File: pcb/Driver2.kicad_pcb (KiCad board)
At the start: 2 copper layers, 78 x 124 mm, 27 parts, among them P1 CONN_2, P2 CONN_2, Q1 IRF540N, Q2 IRF540N, T1 ETD29, U1 ArdinoMinPro, U2 MCP14E3

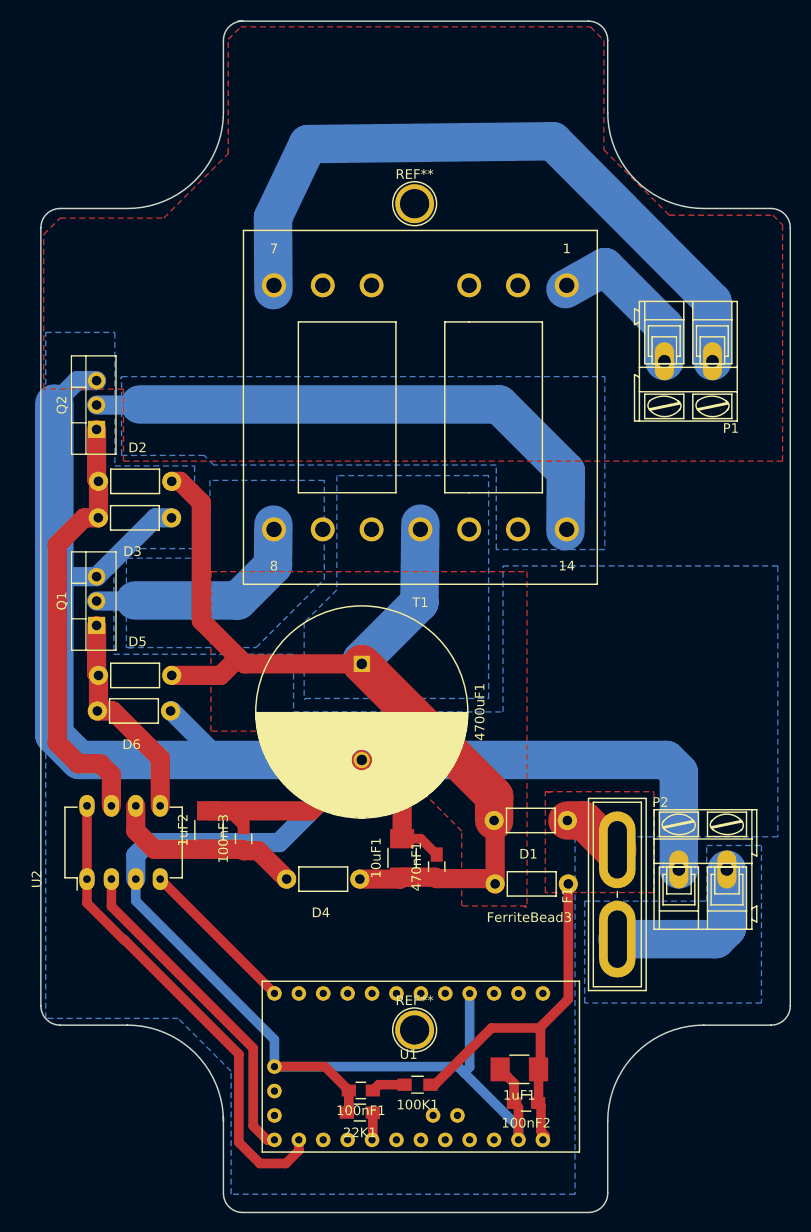
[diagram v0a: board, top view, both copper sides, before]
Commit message: Rev 1 working code, schematic updated, pcb todo
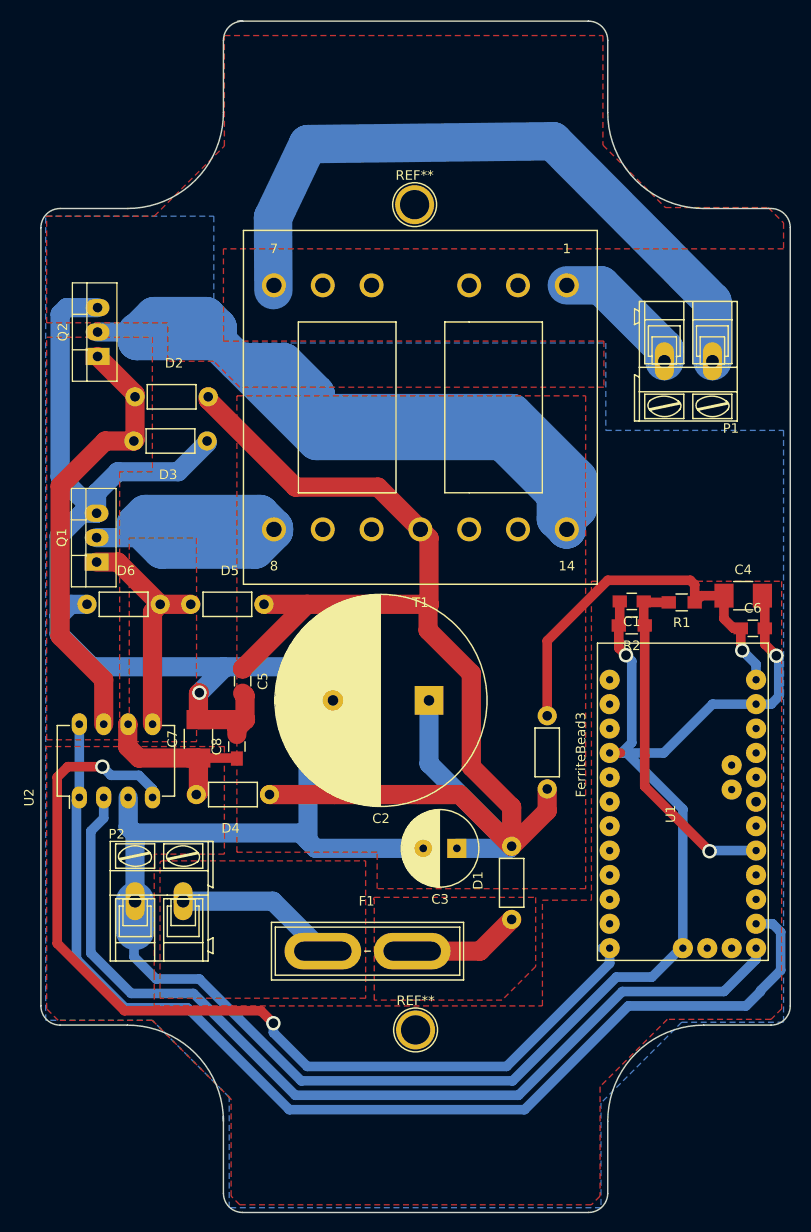
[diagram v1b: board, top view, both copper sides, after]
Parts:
- removed 100K1, 22K1: R, Resistors_SMD:R_0805_HandSoldering
- removed 100nF1, 100nF2, 100nF3, 470nF1: C, Capacitors_SMD:C_0805_HandSoldering
- removed 10uF1, 1uF1, 1uF2: CAPAPOL, Capacitors_SMD:C_1210_HandSoldering
- removed 4700uF1: CAPAPOL, Capacitors_ThroughHole:C_Radial_D22_L41_P10
- removed the REF** at (137.4, 160.5)
- removed the REF** at (137.4, 74.5)
- added C1: 100nF, Capacitors_SMD:C_0805_HandSoldering, F.Cu at (160.0, 115.9)
- added C2: 4700uF 50V, Capacitors_ThroughHole:C_Radial_D22_L41_P10, F.Cu at (138.9, 126.2)
- added C3: 330uF 50v, Capacitors_ThroughHole:C_Radial_D8_L11.5_P3.5, F.Cu at (141.8, 141.6)
- added C4: 1uF, Capacitors_SMD:C_1210_HandSoldering, F.Cu at (171.6, 115.3)
- added C5: 470nF, Capacitors_SMD:C_0805_HandSoldering, F.Cu at (119.5, 124.2)
- added C6: 100nF, Capacitors_SMD:C_0805_HandSoldering, F.Cu at (172.6, 118.7)
- added C7: 1uF, Capacitors_SMD:C_1210_HandSoldering, F.Cu at (114.9, 130.2)
- added C8: 100nF, Capacitors_SMD:C_0805_HandSoldering, F.Cu at (118.9, 131.0)
- added R1: 100K, Resistors_SMD:R_0805_HandSoldering, F.Cu at (165.2, 116.0)
- added R2: 22K, Resistors_SMD:R_0805_HandSoldering, F.Cu at (160.0, 118.4)
- added REF**: 1pin, Connect:1pin, F.Cu at (137.5, 160.5)
- added REF**: 1pin, Connect:1pin, F.Cu at (137.4, 74.6)
- U2: value MCP14E3 -> MCP14E4
- moved P2 56.7 mm to (108.3, 147.1)
- moved U1 46.9 mm to (170.4, 130.4), turned to 270 degrees
- moved F1 26.7 mm to (132.5, 152.3), turned to 0 degrees
- moved FerriteBead3 17.6 mm to (151.2, 127.8), turned to 270 degrees
- moved D6 14.1 mm to (103.3, 116.2), turned to 0 degrees
- moved D4 12.9 mm to (122.3, 136.0)
- moved D5 12.1 mm to (114.1, 116.2)
- moved D1 11.8 mm to (147.5, 149.0), turned to 90 degrees
- moved D2 9.59 mm to (108.3, 94.6)
- moved D3 8.81 mm to (115.8, 99.2)
- moved U2 8.54 mm to (102.5, 136.3)
- moved Q2 7.60 mm to (104.4, 90.4)
- moved Q1 6.60 mm to (104.3, 111.8)
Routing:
- net Net-(Q2-Pad2): track 58.0 -> 176.9 mm
- net PWMB: track 16.8 -> 99.7 mm, vias 0 -> 2
- net ENPWM: track 50.4 -> 117.7 mm
- net PWMA: track 34.6 -> 99.7 mm
- net 12vPower: track 102.7 -> 151.8 mm
- net ADC1: track 6.42 -> 36.3 mm, vias 0 -> 1
- net Net-(Q1-Pad2): track 24.1 -> 50.8 mm
- net Net-(D1-Pad1): track 6.46 -> 11.7 mm
- net GND: track 314.9 -> 317.9 mm, vias 0 -> 3
- net Net-(P1-Pad2): track 17.1 -> 14.2 mm
- net Net-(C7-Pad1): track 20.4 -> 18.2 mm
- net Net-(D5-Pad1): track 22.6 -> 24.4 mm
- net Net-(F1-Pad1): track 18.0 -> 16.7 mm
- net Net-(D2-Pad1): track 45.6 -> 46.8 mm
- net 12v: track 41.5 -> 41.9 mm, vias 0 -> 1
- added copper zone on F.Cu, net Net-(D1-Pad1)
- added copper zone on F.Cu, net Net-(D5-Pad1)
- added copper zone on F.Cu, net Net-(F1-Pad1)
- removed copper zone on B.Cu, net 12vPower
- removed copper zone on B.Cu, net Net-(F1-Pad1)
- removed copper zone on B.Cu, net Net-(Q1-Pad2)
- removed copper zone on B.Cu, net Net-(Q2-Pad2)
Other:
- net class Default: via_dia 2 -> 1.5

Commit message: Added loadswitch to avoid inrush
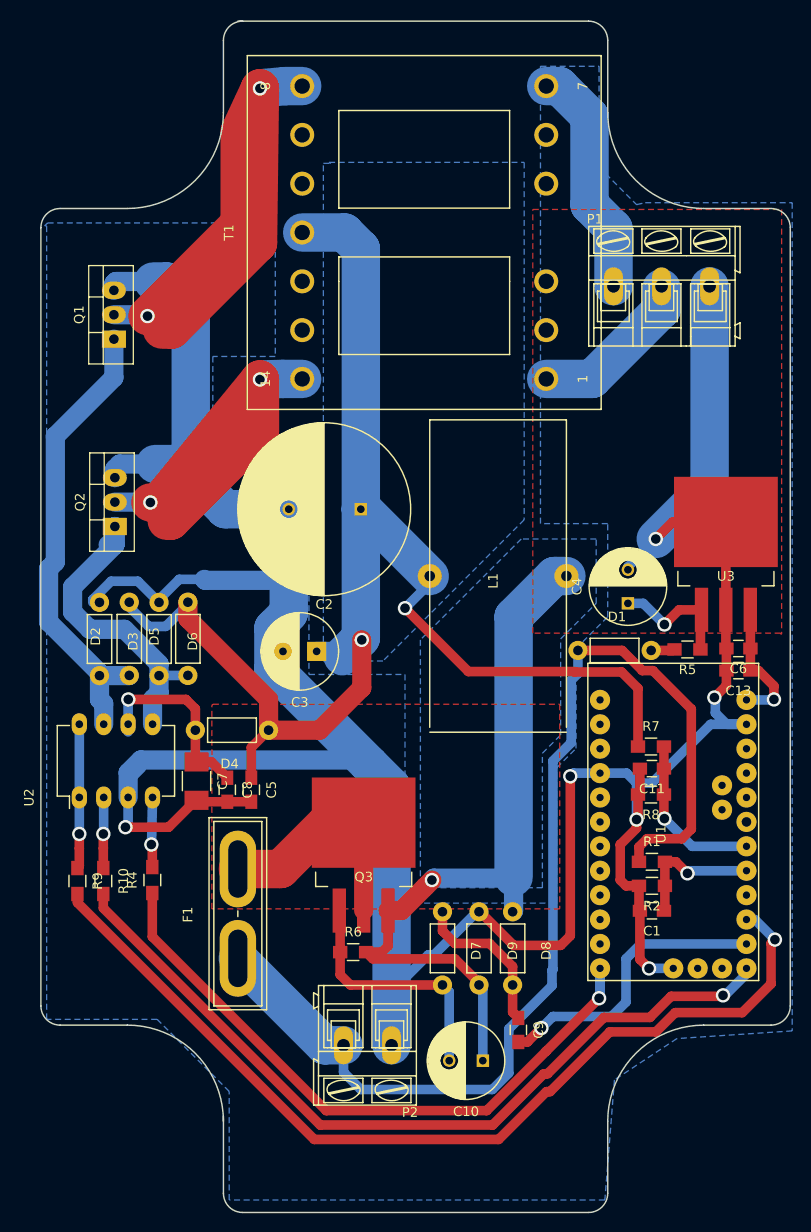
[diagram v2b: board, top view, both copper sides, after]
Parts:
- removed FerriteBead3: INDUCTOR, Resistors_ThroughHole:Resistor_Horizontal_RM7mm
- removed REF** (x2): 1pin, Connect:1pin
- added C10: 10uF, Capacitors_ThroughHole:C_Radial_D8_L11.5_P3.5, F.Cu at (144.5, 163.7)
- added C11: 100nF, Capacitors_SMD:C_0805_HandSoldering, F.Cu at (162.1, 133.3)
- added C13: 100nF, Capacitors_SMD:C_0805_HandSoldering, F.Cu at (171.1, 123.1)
- added C9: 10nF, Capacitors_SMD:C_0805_HandSoldering, F.Cu at (148.2, 160.5)
- added D7: 1N5819, Resistors_ThroughHole:Resistor_Horizontal_RM7mm, F.Cu at (140.3, 148.2)
- added D8: 1N5819, Resistors_ThroughHole:Resistor_Horizontal_RM7mm, F.Cu at (147.6, 148.2)
- added D9: 1N5819, Resistors_ThroughHole:Resistor_Horizontal_RM7mm, F.Cu at (144.1, 148.2)
- added L1: 330uH 5A TBC, Divers:Choke14x32, F.Cu at (153.2, 97.0)
- added Q3: IRF540N, TO_SOT_Packages_SMD:TO-263-3Lead, F.Cu at (132.1, 143.5)
- added R10: 120R, Resistors_SMD:R_0805_HandSoldering, F.Cu at (105.0, 145.0)
- added R4: 120R, Resistors_SMD:R_0805_HandSoldering, F.Cu at (110.1, 144.9)
- added R5: 22R, Resistors_SMD:R_0805_HandSoldering, F.Cu at (165.8, 120.9)
- added R6: 100K, Resistors_SMD:R_0805_HandSoldering, F.Cu at (131.0, 152.4)
- added R7: 100K, Resistors_SMD:R_0805_HandSoldering, F.Cu at (162.0, 131.0)
- added R8: 22K, Resistors_SMD:R_0805_HandSoldering, F.Cu at (162.0, 136.0)
- added R9: 120R, Resistors_SMD:R_0805_HandSoldering, F.Cu at (102.3, 145.0)
- added U3: LM7808ACT, TO_SOT_Packages_SMD:TO-263-3Lead, F.Cu at (169.8, 112.2)
- C2: footprint Capacitors_ThroughHole:C_Radial_D22_L41_P10 -> Capacitors_ThroughHole:C_Radial_D18_L36_P7.5
- C4: value 1uF -> 100uF; footprint Capacitors_SMD:C_1210_HandSoldering -> Capacitors_ThroughHole:C_Radial_D8_L11.5_P3.5
- C6: value 100nF -> 1uF
- P1: footprint Connect:AK300-2 -> Connect:AK300-3
- Q1, Q2: value IRF540N -> RPF60N06
- moved C1 32.3 mm to (162.1, 148.1)
- moved P2 30.6 mm to (135.0, 162.1), turned to 180 degrees
- moved D2 29.0 mm to (107.7, 123.6), turned to 90 degrees
- moved D1 28.8 mm to (154.4, 121.0), turned to 0 degrees
- moved R2 27.2 mm to (162.1, 145.5)
- moved R1 27.2 mm to (162.1, 143.0), turned to 0 degrees
- moved C3 25.2 mm to (127.2, 121.1)
- moved Q1 23.3 mm to (106.1, 88.6)
- moved C2 21.1 mm to (131.8, 106.3)
- moved D3 20.2 mm to (104.6, 116.0), turned to 270 degrees
- moved T1 18.2 mm to (138.4, 77.5), turned to 90 degrees
- moved Q2 17.8 mm to (106.2, 108.1)
- moved F1 14.1 mm to (119.0, 148.4), turned to 90 degrees
- moved P1 12.9 mm to (158.1, 83.1), turned to 0 degrees
- moved C4 12.0 mm to (159.6, 116.1), turned to 90 degrees
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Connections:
- C4 pad 1: 12v -> Net-(C4-Pad1)
- C6 pad 1: 12v -> 8v
- D1 pad 1: Net-(D1-Pad1) -> 12v
- D1 pad 2: 12vPower -> Net-(D1-Pad2)
- F1 pad 1: Net-(F1-Pad1) -> 12v
- F1 pad 2: Net-(D1-Pad1) -> Net-(F1-Pad2)
- P2 pad 2: Net-(F1-Pad1) -> 12v
- Q1 pad 1: Net-(D5-Pad1) -> Net-(D2-Pad1)
- Q2 pad 1: Net-(D2-Pad1) -> Net-(D5-Pad1)
- U1 pad 12: PWMB -> Net-(R4-Pad1)
- U1 pad 13: PWMA -> Net-(R10-Pad2)
- U1 pad 14: ENPWM -> PWRENABLE
- U1 pad 15: (no net) -> Net-(R9-Pad2)
- U1 pad 18: (no net) -> ADC2
- U1 pad 24: 12v -> 8v
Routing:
- net Net-(Q2-Pad2): track 176.9 -> 44.5 mm, vias 0 -> 2
- net ENPWM: track 117.7 -> 15.1 mm, vias 0 -> 1
- net Net-(R9-Pad2): track 0.00 -> 98.6 mm, vias 0 -> 1
- net PWMB: track 99.7 -> 7.28 mm, vias 2 -> 1
- net PWMA: track 99.7 -> 7.37 mm, vias 0 -> 1
- net Net-(R10-Pad2): track 0.00 -> 84.9 mm, vias 0 -> 1
- net Net-(C10-Pad1): track 0.00 -> 80.0 mm, vias 0 -> 1
- net 12v: track 41.9 -> 117.8 mm, vias 1 -> 0
- net Net-(R4-Pad1): track 0.00 -> 69.6 mm, vias 0 -> 1
- net Net-(P1-Pad1): track 71.3 -> 24.5 mm
- net GND: track 317.9 -> 361.1 mm, vias 3 -> 6
- net PWRENABLE: track 0.00 -> 30.6 mm, vias 0 -> 1
- net Net-(C10-Pad2): track 0.00 -> 26.0 mm
- net Net-(F1-Pad2): track 0.00 -> 24.2 mm
- net ADC1: track 36.3 -> 14.2 mm
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- added copper zone on B.Cu, net 12vPower
- added copper zone on B.Cu, net Net-(C10-Pad1)
- added copper zone on F.Cu, net Net-(F1-Pad2)
- removed copper zone on F.Cu, net 12vPower
- removed copper zone on F.Cu, net Net-(D1-Pad1)
- removed copper zone on F.Cu, net Net-(D2-Pad1)
- removed copper zone on F.Cu, net Net-(D5-Pad1)
- removed copper zone on F.Cu, net Net-(F1-Pad1)
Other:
- net class Default: trace_width 1 -> 4

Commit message: Working version with soft start, some frequency adjustments to come
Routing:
- net GND: track 361.1 -> 416.7 mm
- net Net-(C10-Pad1): track 80.0 -> 92.7 mm
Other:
- net class Default: trace_width 4 -> 2
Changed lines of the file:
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@@
     (thickness 1.6)
     (drawings 57)
-    (tracks 365)
+    (tracks 382)
     (zones 0)
     (modules 41)
@@
   )
   (setup
-    (last_trace_width 4)
+    (last_trace_width 2)
     (trace_clearance 0.5)
     (zone_clearance 1)
@@
   (net_class Default "This is the default net class."
     (clearance 0.5)
-    (trace_width 4)
+    (trace_width 2)
     (via_dia 1.5)
     (via_drill 1)
@@
   (gr_line (start 99 179.5) (end 176 179.5) (angle 90) (layer Dwgs.User) (width 0.2))
   (gr_line (start 176 55.5) (end 99 55.5) (angle 90) (layer Dwgs.User) (width 0.2))
-  (segment (start 168.1 83.1) (end 168.1 103.8) (width 4) (layer B.Cu) (net 1))
+  (segment (start 128.9 129.1) (end 130.8 129.1) (width 4) (layer B.Cu) (net 1))
+  (segment (start 167.5 91.2) (end 168.1 91.2) (width 4) (layer B.Cu) (net 1))
+  (segment (start 142.7 116) (end 167.5 91.2) (width 4) (layer B.Cu) (net 1))
+  (segment (start 142.7 117.2) (end 142.7 116) (width 4) (layer B.Cu) (net 1))
+  (segment (start 130.8 129.1) (end 142.7 117.2) (width 4) (layer B.Cu) (net 1))
+  (segment (start 168.1 83.1) (end 168.1 91.2) (width 4) (layer B.Cu) (net 1))
+  (segment (start 168.1 91.2) (end 168.1 103.8) (width 4) (layer B.Cu) (net 1))
   (segment (start 168.1 103.8) (end 162.5 109.4) (width 4) (layer B.Cu) (net 1))
   (segment (start 124.3 113.7) (end 115.6 113.7) (width 2) (layer B.Cu) (net 1))
@@
   (segment (start 124.3 117.1) (end 122.7 118.7) (width 4) (layer B.Cu) (net 1))
   (segment (start 122.7 118.7) (end 122.7 122.9) (width 4) (layer B.Cu) (net 1))
-  (segment (start 122.7 122.9) (end 132.7 132.9) (width 4) (layer B.Cu) (net 1))
+  (segment (start 122.7 122.9) (end 128.9 129.1) (width 4) (layer B.Cu) (net 1))
+  (segment (start 128.9 129.1) (end 132.7 132.9) (width 4) (layer B.Cu) (net 1))
   (segment (start 135 135.2) (end 135 162.1) (width 4) (layer B.Cu) (net 1))
   (segment (start 132.7 132.9) (end 135 135.2) (width 4) (layer B.Cu) (net 1))
@@
   (segment (start 159.4 153.1) (end 159.4 157.6) (width 1) (layer B.Cu) (net 18))
   (segment (start 160.95 151.55) (end 159.4 153.1) (width 1) (layer B.Cu) (net 18))
-  (segment (start 138.5 145.6) (end 139.2 144.9) (width 2) (layer F.Cu) (net 19))
-  (via (at 139.2 144.9) (size 1.5) (drill 1) (layers F.Cu B.Cu) (net 19))
-  (segment (start 139.4 144.7) (end 147.7 144.7) (width 2) (layer B.Cu) (net 19))
-  (segment (start 139.2 144.9) (end 139.4 144.7) (width 2) (layer B.Cu) (net 19))
+  (segment (start 139.25 144.85) (end 141.25 144.85) (width 2) (layer F.Cu) (net 19))
+  (segment (start 141.25 144.85) (end 141.5 144.6) (width 2) (layer F.Cu) (net 19))
+  (segment (start 139.25 144.85) (end 139.25 142.65) (width 2) (layer F.Cu) (net 19))
+  (segment (start 139.5 142.9) (end 141.2 142.9) (width 2) (layer F.Cu) (net 19))
+  (segment (start 139.25 142.65) (end 139.5 142.9) (width 2) (layer F.Cu) (net 19))
+  (segment (start 137.5 146.7) (end 135.7 148.5) (width 2) (layer F.Cu) (net 19))
+  (segment (start 137.5 146.05) (end 137.5 146.7) (width 2) (layer F.Cu) (net 19))
+  (segment (start 137.5 146.7) (end 137.5 148.2) (width 2) (layer F.Cu) (net 19))
+  (segment (start 137.5 148.2) (end 135.4 150.3) (width 2) (layer F.Cu) (net 19))
+  (segment (start 138.05 146.05) (end 137.5 146.05) (width 2) (layer F.Cu) (net 19))
+  (segment (start 137.5 146.05) (end 136.665 146.05) (width 2) (layer F.Cu) (net 19))
+  (segment (start 136.665 146.05) (end 134.64 148.075) (width 2) (layer F.Cu) (net 19))
+  (via (at 141.2 142.9) (size 1.5) (drill 1) (layers F.Cu B.Cu) (net 19))
+  (segment (start 141.4 142.7) (end 147.7 144.7) (width 2) (layer B.Cu) (net 19))
+  (segment (start 141.2 142.9) (end 141.4 142.7) (width 2) (layer B.Cu) (net 19))
   (segment (start 147.7 148.1) (end 147.7 144.7) (width 2) (layer B.Cu) (net 19))
   (segment (start 147.7 144.7) (end 147.7 144.6) (width 2) (layer B.Cu) (net 19))
@@
   (segment (start 151.944 113.256) (end 153.2 113.256) (width 4) (layer B.Cu) (net 19))
   (segment (start 147.7 148.1) (end 147.6 148.2) (width 2) (layer B.Cu) (net 19))
-  (segment (start 136.025 148.075) (end 134.64 148.075) (width 2) (layer F.Cu) (net 19))
-  (segment (start 138.5 145.6) (end 136.025 148.075) (width 2) (layer F.Cu) (net 19))
+  (segment (start 139.25 144.85) (end 138.05 146.05) (width 2) (layer F.Cu) (net 19))
   (segment (start 132.35 152.4) (end 134 152.4) (width 1) (layer F.Cu) (net 19))
   (segment (start 134 152.4) (end 134.64 151.76) (width 1) (layer F.Cu) (net 19))
@@
     (polygon
       (pts
-        (xy 99.2 76.5) (xy 122.9 76.5) (xy 122.9 90.4) (xy 116.4 90.4) (xy 116.4 101.3)
+        (xy 98.7 55.6) (xy 149.3 55.3) (xy 149.3 63.5) (xy 124.3 63.6) (xy 124.8 101.1)
         (xy 126.4 101.3) (xy 126.4 123.5) (xy 136.4 123.5) (xy 136.4 147.3) (xy 152.2 147.3)
         (xy 152.2 133.2) (xy 154.2 131.2) (xy 154.2 120.8) (xy 157.5 117.5) (xy 157.5 107.8)
@@
     (polygon
       (pts
-        (xy 175.5 119.2) (xy 149.7 119.2) (xy 149.7 75.1) (xy 175.6 75.1) (xy 175.6 119.3)
+        (xy 175.5 119.2) (xy 99.4 119.1) (xy 99 55.5) (xy 175.2 55.6) (xy 175.6 119.3)
         (xy 175.5 119.3)
       )
